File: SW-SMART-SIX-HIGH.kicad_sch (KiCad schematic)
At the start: 53 parts, among them J1 SWLINK, J2 USART1, J3 POWER OUT, J4 POWER IN, SW0 BTS7002-1EPP, SW1 BTS7002-1EPP, SW2 BTS7002-1EPP, U1 STM32G0B1KBTx, U4 MCP2562-E-SN

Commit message: lots of work to do!
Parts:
- removed CVIN1: 10u, Capacitor_SMD:C_1206_3216Metric_Pad1.33x1.80mm_HandSolder, symbol Device:C_Small
- removed VR5V0: NCV1117ST50, PCM_SparkFun-Semiconductor-Standard:SOT-223-3_TabPin2, symbol PCM_SparkFun-Regulator:LM1117-3.3
- added C15, CIN2: 100n, Capacitor_SMD:C_0603_1608Metric_Pad1.08x0.95mm_HandSolder, symbol Device:C_Small
- added CIN1: 10u, Capacitor_SMD:C_1210_3225Metric_Pad1.33x2.70mm_HandSolder, symbol Device:C_Small
- added COUT3, COUT4: 10u, Capacitor_SMD:C_0805_2012Metric_Pad1.18x1.45mm_HandSolder, symbol Device:C_Small
- added COUT5, COUT6, COUT7: 10n, Capacitor_SMD:C_0603_1608Metric_Pad1.08x0.95mm_HandSolder, symbol Device:C_Small
- added J5: POWER OUT, TerminalBlock_Phoenix:TerminalBlock_Phoenix_MKDS-3-5-5.08_1x05_P5.08mm_Horizontal, symbol Connector:Screw_Terminal_01x05
- added L1: 8.2 uH 55.2 mOhm, SRP5030HMT2R2M, symbol SamacSys_Parts:SRP5030HMT-8R2M
- added R13, R14, R16, R17, R19, R20: 4K7, Resistor_SMD:R_0603_1608Metric_Pad0.98x0.95mm_HandSolder, symbol Device:R_Small_US
- added R15, R18, R21: 10K, Resistor_SMD:R_0603_1608Metric_Pad0.98x0.95mm_HandSolder, symbol Device:R_Small_US
- added R22, R23, R24: 1K0, Resistor_SMD:R_0603_1608Metric_Pad0.98x0.95mm_HandSolder, symbol Device:R_Small_US
- added RFBT1: 115K, Resistor_SMD:R_0603_1608Metric_Pad0.98x0.95mm_HandSolder, symbol Device:R_US
- added RGND3, RGND4, RGND5: 47R, Resistor_SMD:R_0603_1608Metric_Pad0.98x0.95mm_HandSolder, symbol Device:R_Small_US
- added RPD3, RPD4, RPD5: 47K, Resistor_SMD:R_0603_1608Metric_Pad0.98x0.95mm_HandSolder, symbol Device:R_Small_US
- added RRFBB1: 22K1, Resistor_SMD:R_0603_1608Metric_Pad0.98x0.95mm_HandSolder, symbol Device:R_US
- added SW3, SW4, SW5: BTS7002-1EPP, SamacSys_Parts:SOP65P600X115-15N, symbol Power_Management:BTS7004-1EPP
- added U3: LMR54410, Package_TO_SOT_SMD:SOT-23-6, symbol Regulator_Switching:LMR50410
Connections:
- net +12V: now also CIN1.1, CIN2.1, SW3.15 (VS), SW4.15 (VS), SW5.15 (VS), U3.4 (EN), U3.5 (VIN)
- net +5V: now also COUT3.1, COUT4.1, L1.2, RFBT1.1
- net GND: now also CIN1.2, CIN2.2, COUT3.2, COUT4.2, COUT5.2, COUT6.2, COUT7.2, R22.1, R23.1, R24.1, RGND3.2, RGND4.2, RGND5.2, RPD3.1, RPD4.1, RPD5.1, RRFBB1.1, U3.2 (GND)
- net SW0DEN: now also R20.1; no longer R10.1, U1.31 (PB7)
- net SW0IN: now also R19.1; no longer R8.1, U1.32 (PB8)
- net SW0IS: now also R21.1; no longer R11.1, U1.9 (PA2)
- net SW2DEN: now also R17.1; no longer R2.1, U1.27 (PB3)
- net SW2IN: now also R16.1; no longer R1.1, U1.28 (PB4)
- net SW2IS: now also R18.1; no longer R6.1, U1.8 (PA1)
- net SW0IS_PD renamed SWIS_PD0
- net SW0OUT renamed SWOUT0
- net SWOUT0: no longer J3.5 (Pin_5)
- net SW1DEN renamed SWDEN1
- net SW1IN renamed SWIN1
- net SW1IS renamed SWIS1
- net SW1IS_PD renamed SWIS_PD1
- net SW1OUT renamed SWOUT1
- net SWOUT1: no longer J3.3 (Pin_3)
- net SW2IS_PD renamed SWIS_PD2
- net SW2OUT renamed SWOUT2
- net SWOUT2: no longer J3.1 (Pin_1)
- new net: RGND5.1, SW5.1 (GND)
- new net: RGND3.1, SW3.1 (GND)
- new net: R13.2, SW3.2 (IN)
- new net: R14.2, SW3.3 (DEN)
- new net: R19.2, SW5.2 (IN)
- new net: R20.2, SW5.3 (DEN)
- new net: RGND4.1, SW4.1 (GND)
- new net: R16.2, SW4.2 (IN)
- new net: R17.2, SW4.3 (DEN)
- new net: RFBT1.2, RRFBB1.2, U3.3 (FB)
- new net CB: C15.1, U3.1 (CB)
- new net SW: C15.2, L1.1, U3.6 (SW)
- new net SW3DEN: R14.1
- new net SW3IN: R13.1
- new net SW3IS: R15.1
- new net SWDEN0: R10.1, U1.31 (PB7)
- new net SWDEN2: R2.1, U1.27 (PB3)
- new net SWIN0: R8.1, U1.32 (PB8)
- new net SWIN2: R1.1, U1.28 (PB4)
- new net SWIS0: R11.1, U1.9 (PA2)
- new net SWIS2: R6.1, U1.8 (PA1)
- new net SWIS_PD3: R15.2, R22.2, SW3.4 (IS)
- new net SWIS_PD4: R18.2, R23.2, SW4.4 (IS)
- new net SWIS_PD5: R21.2, R24.2, SW5.4 (IS)
- new net SWOUT3: COUT5.1, RPD3.2, SW3.10 (OUT), SW3.12 (OUT), SW3.13 (OUT), SW3.14 (OUT), SW3.8 (OUT), SW3.9 (OUT)
- new net SWOUT4: COUT6.1, RPD4.2, SW4.10 (OUT), SW4.12 (OUT), SW4.13 (OUT), SW4.14 (OUT), SW4.8 (OUT), SW4.9 (OUT)
- new net SWOUT5: COUT7.1, RPD5.2, SW5.10 (OUT), SW5.12 (OUT), SW5.13 (OUT), SW5.14 (OUT), SW5.8 (OUT), SW5.9 (OUT)
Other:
- title: Smart Triple High Side Switch -> Smart Six Way High Side Switch
- moved on the sheet: COUT0, H1, H2, H3, H4, R10, R11, R12, R8, RGND0, RPD0, SW0

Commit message: added ACS712 to monitor total board current
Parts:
- added H5, H6: M4 4.3mm, MountingHole:MountingHole_4.3mm_M4, symbol Mechanical:MountingHole
- added U2: ACS71240LLCBTR-050B3, Package_SO:SOIC-8_3.9x4.9mm_P1.27mm, symbol Sensor_Current:ACS712xLCTR-30A
- J1: footprint PCM_SparkFun-Connector:1x05_P2.54mm_Locking -> Connector_PinHeader_2.54mm:PinHeader_1x05_P2.54mm_Vertical
- J2: footprint PCM_SparkFun-Connector:1x04_P2.54mm_Locking -> Connector_PinHeader_2.54mm:PinHeader_1x04_P2.54mm_Vertical
- renumbered COUT3 to C5V2, COUT4 to C5V3, COUT5 to COUT3, COUT6 to COUT4, COUT7 to COUT5
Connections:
- net +12V: now also U2.3 (IP-), U2.4 (IP-); no longer D1.2 (A2), J4.1, J4.2
- net +3.3V: now also U2.8 (VCC)
- net GND: now also U2.5 (GND)
- net SWOUT0: now also J3.5 (Pin_5)
- net SWOUT1: now also J3.3 (Pin_3)
- net SWOUT2: now also J3.1 (Pin_1)
- net SWOUT3: now also J5.1 (Pin_1)
- net SWOUT4: now also J5.3 (Pin_3)
- net SWOUT5: now also J5.5 (Pin_5)
- net IS_TOT: now reaches U1.11 (PA4)
- net IS_TOT: now also U2.7 (VIOUT)
- net SW0DEN renamed SWDEN5
- net SW0IN renamed SWIN5
- net SW0IS renamed SWIS5
- net SW2DEN renamed SWDEN4
- net SW2IN renamed SWIN4
- net SW2IS renamed SWIS4
- net SW3DEN renamed SWDEN3
- net SW3IN renamed SWIN3
- net SW3IS renamed SWIS3
- new net VBAT: D1.2 (A2), J4.1, J4.2, U2.1 (IP+), U2.2 (IP+)
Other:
- moved on the sheet: D1

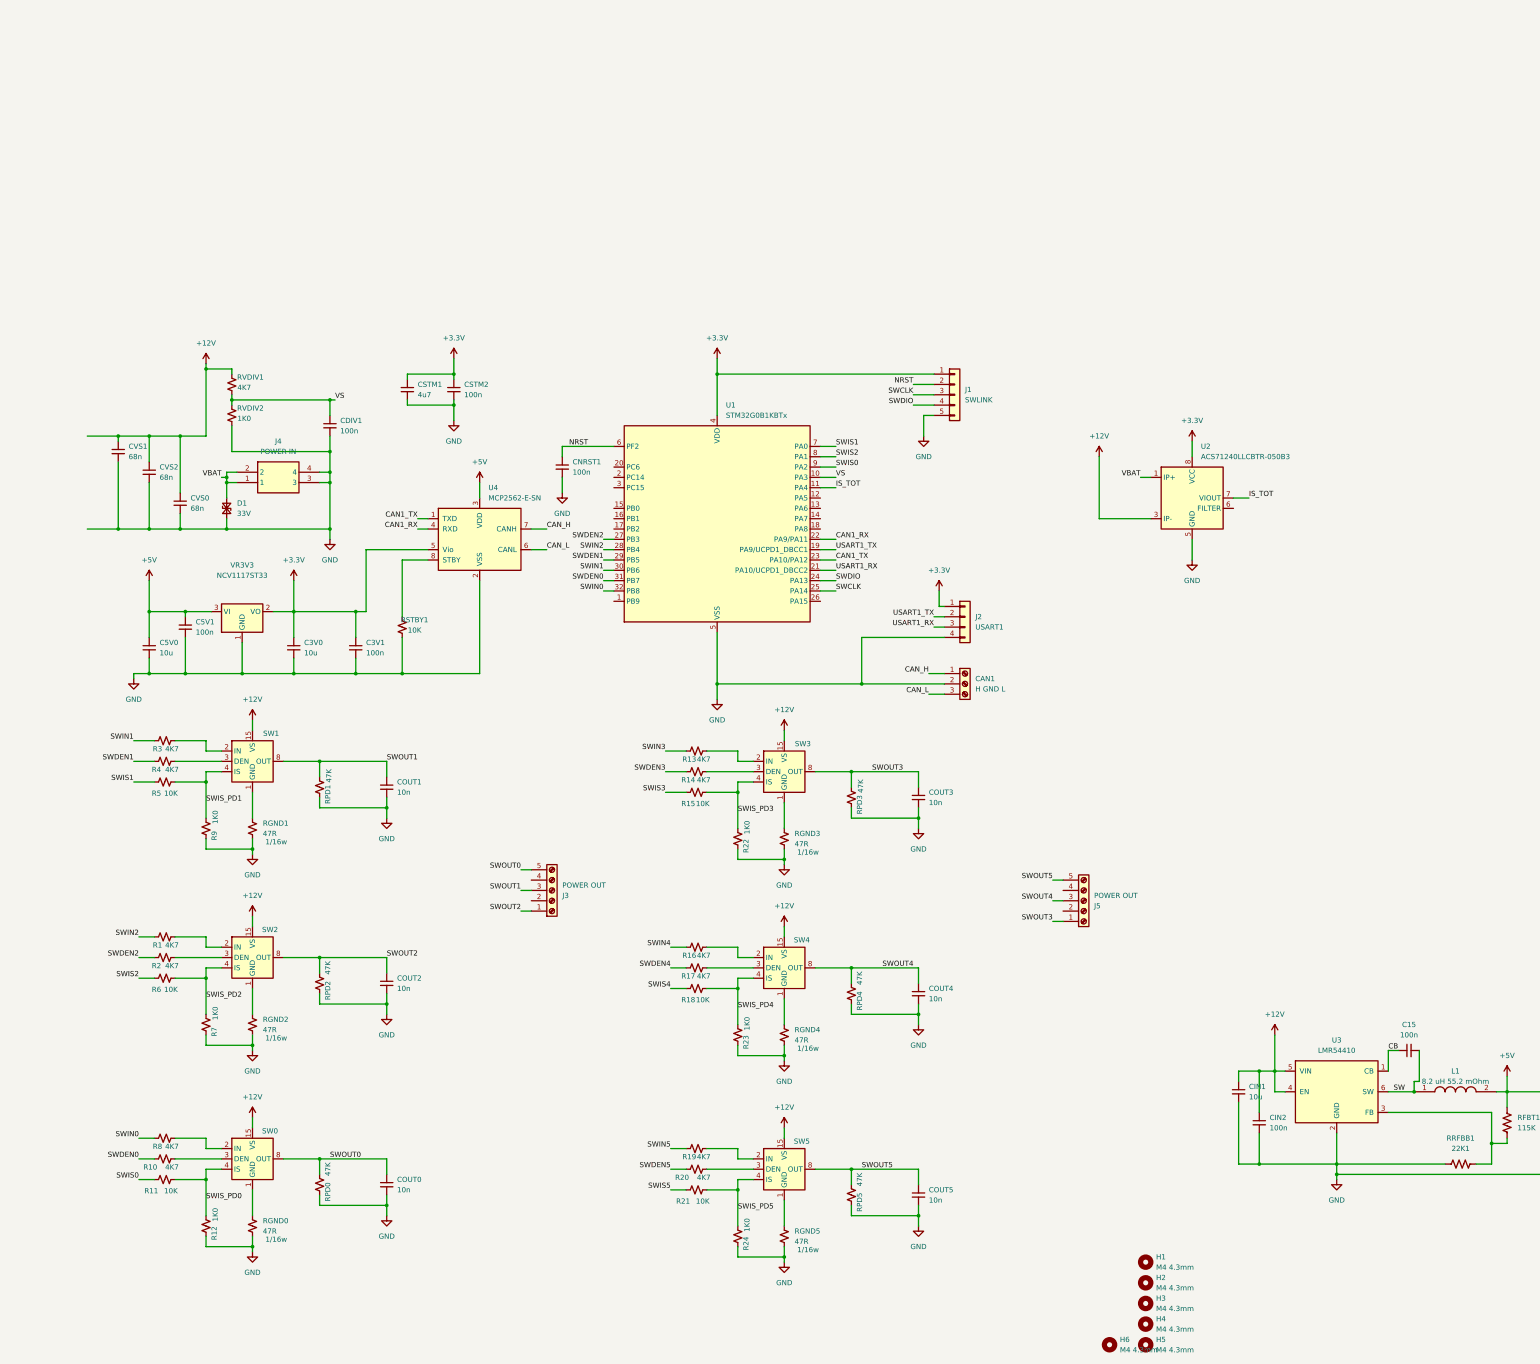
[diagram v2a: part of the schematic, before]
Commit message: swapped to a 48pin uC
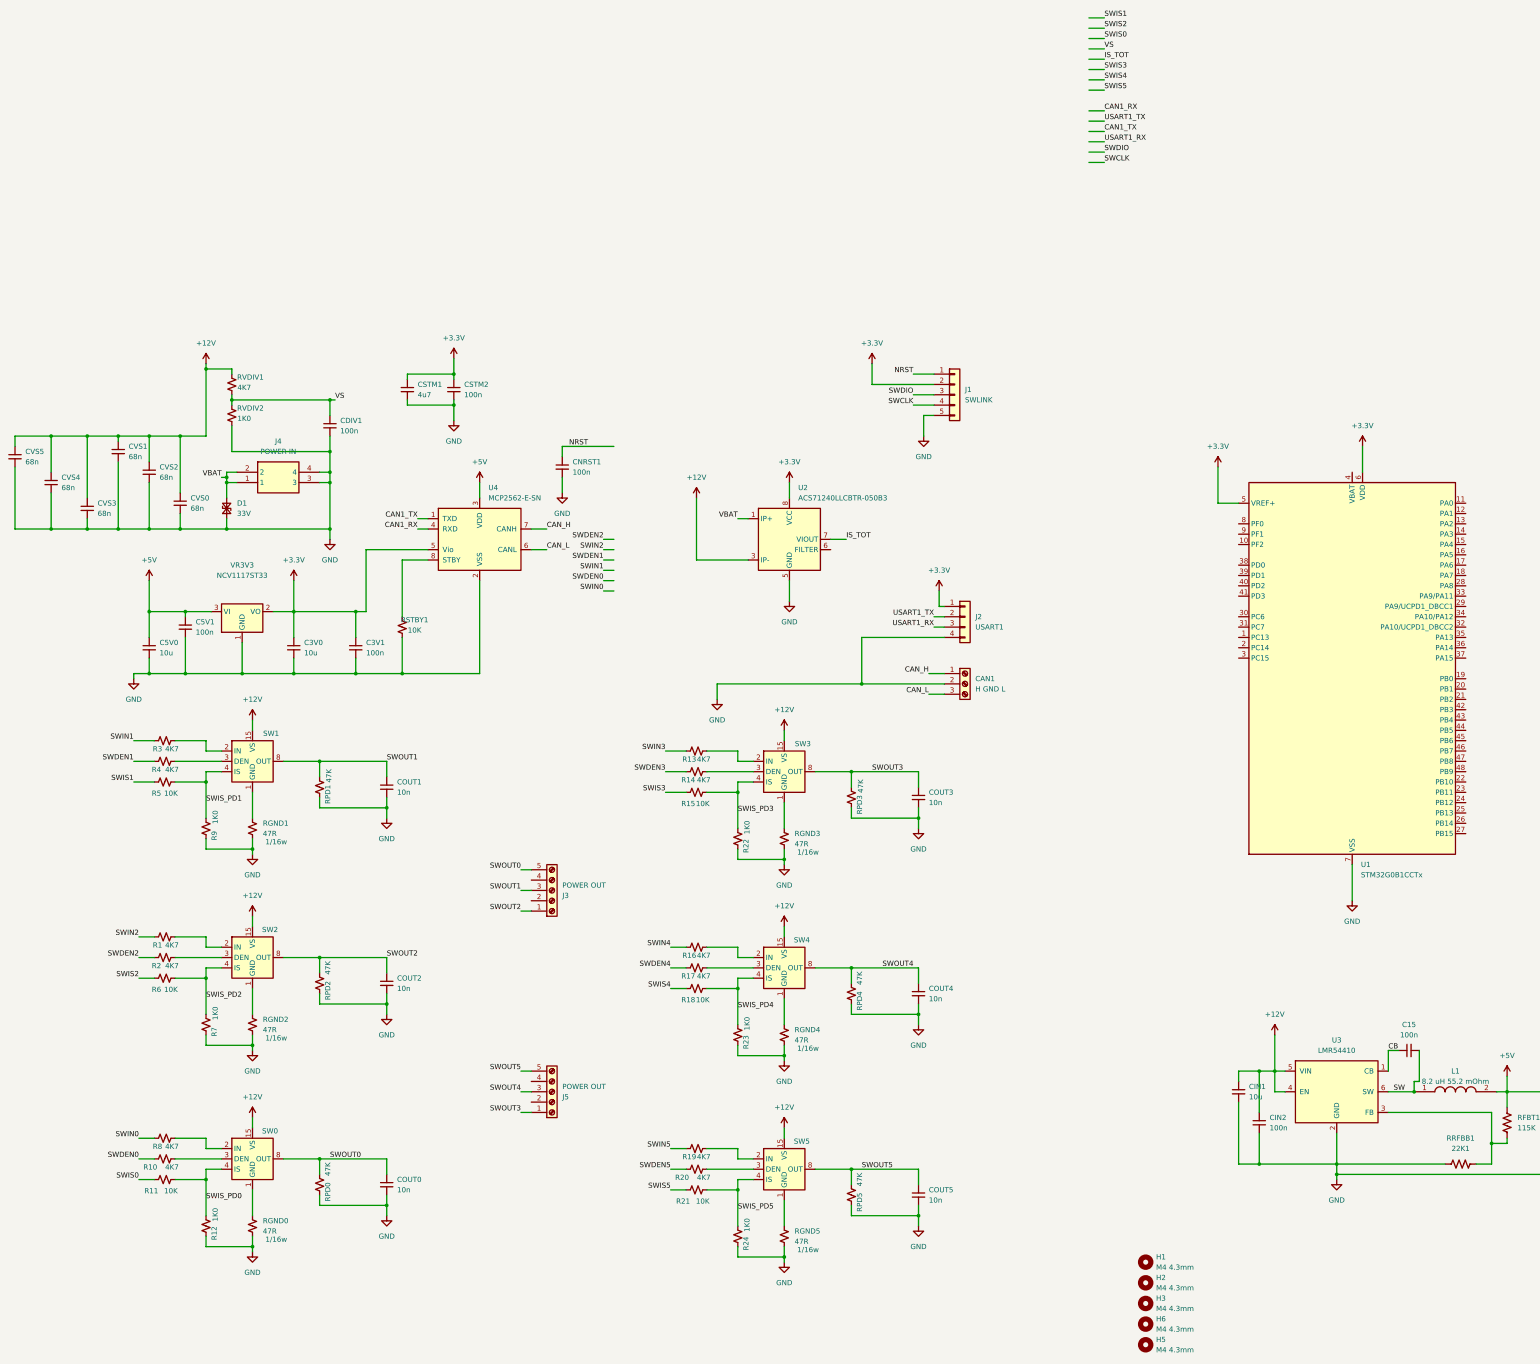
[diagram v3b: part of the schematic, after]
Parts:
- removed H4: M4 4.3mm, MountingHole:MountingHole_4.3mm_M4, symbol Mechanical:MountingHole
- removed U1: STM32G0B1KBTx, Package_QFP:LQFP-32_7x7mm_P0.8mm, symbol MCU_ST_STM32G0:STM32G0B1KBTx
- added CVS3, CVS4, CVS5: 68n, Capacitor_SMD:C_0603_1608Metric_Pad1.08x0.95mm_HandSolder, symbol Device:C_Small
- added U1: STM32G0B1CCTx, Package_QFP:LQFP-48_7x7mm_P0.5mm, symbol MCU_ST_STM32G0:STM32G0B1CCTx
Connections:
- net +12V: now also CVS3.1, CVS4.1, CVS5.1
- net +3.3V: now also J1.2 (Pin_2), U1.5 (VREF+), U1.6 (VDD); no longer J1.1 (Pin_1)
- net GND: now also CVS3.2, CVS4.2, CVS5.2, U1.7 (VSS)
- net NRST: now also J1.1 (Pin_1); no longer J1.2 (Pin_2)
- net SWCLK: now also J1.4 (Pin_4); no longer J1.3 (Pin_3)
- net SWDIO: now also J1.3 (Pin_3); no longer J1.4 (Pin_4)
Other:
- moved on the sheet: H6, J5, U2

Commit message: lots of work to do still
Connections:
- net CAN1_RX: no longer U4.4 (RXD)
- net CAN1_TX: no longer U4.1 (TXD)
- net NRST: now also U1.10 (PF2)
- net SWDEN0: now also U1.13 (PA2)
- net SWIN0: now also U1.14 (PA3)
- net SWIS0: now also U1.12 (PA1)
- net SWIS1: now also U1.11 (PA0)
- net USART1_RX: now also U1.26 (PB14)
- net USART1_TX: now also U1.25 (PB13)
- net CAN_RX: now reaches U1.19 (PB0)
- net CAN_RX: now also U4.4 (RXD)
- net CAN_TX: now reaches U1.20 (PB1)
- net CAN_TX: now also U4.1 (TXD)
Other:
- note added: "22 PB10 A11 23 PB11 A15 24 PB12 A16 25 PC4 A17 UART1_TX 26 PC5 A18 UART1_RX 15 PB0 A8 16 PB1 A9 17 PB2 A10 07 PA0 A0 08 PA1 A1 09 PA2 A2 10 PA3 A3 11 PA4 A4 12 PA5 A5 13 PA6 A6 14 PA7 A7"
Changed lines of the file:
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@@
 		(company "Gordon McLellan")
 	)
+	(text "22 PB10 A11\n23 PB11 A15\n24 PB12 A16\n\n25 PC4 A17 UART1_TX\n26 PC5 A18 UART1_RX\n\n15 PB0 A8\n16 PB1 A9\n17 PB2 A10\n\n07 PA0 A0\n08 PA1 A1\n09 PA2 A2\n10 PA3 A3\n11 PA4 A4\n12 PA5 A5\n13 PA6 A6\n14 PA7 A7"
+		(exclude_from_sim no)
+		(at 298.704 155.702 0)
+		(effects
+			(font
+				(size 1.27 1.27)
+			)
+		)
+	)
 	(junction
 		(at 92.71 41.91)
@@
 	(wire
 		(pts
+			(xy 311.15 64.77) (xy 316.23 64.77)
+		)
+		(stroke
+			(width 0)
+			(type default)
+		)
+	)
+	(wire
+		(pts
 			(xy 33.02 38.1) (xy 33.02 53.34)
 		)
@@
 	(wire
 		(pts
+			(xy 372.11 57.15) (xy 375.92 57.15)
+		)
+		(stroke
+			(width 0)
+			(type default)
+		)
+	)
+	(wire
+		(pts
 			(xy 114.3 58.42) (xy 116.84 58.42)
 		)
@@
 	(wire
 		(pts
+			(xy 372.11 97.79) (xy 375.92 97.79)
+		)
+		(stroke
+			(width 0)
+			(type default)
+		)
+	)
+	(wire
+		(pts
 			(xy 57.15 87.63) (xy 57.15 96.52)
 		)
@@
 	(wire
 		(pts
+			(xy 372.11 133.35) (xy 375.92 133.35)
+		)
+		(stroke
+			(width 0)
+			(type default)
+		)
+	)
+	(wire
+		(pts
 			(xy 139.7 199.39) (xy 142.24 199.39)
 		)
@@
 	(wire
 		(pts
+			(xy 372.11 100.33) (xy 375.92 100.33)
+		)
+		(stroke
+			(width 0)
+			(type default)
+		)
+	)
+	(wire
+		(pts
 			(xy 78.74 81.28) (xy 83.82 81.28)
 		)
@@
 	(wire
 		(pts
+			(xy 372.11 62.23) (xy 375.92 62.23)
+		)
+		(stroke
+			(width 0)
+			(type default)
+		)
+	)
+	(wire
+		(pts
 			(xy 401.32 213.36) (xy 401.32 210.82)
 		)
@@
 	(wire
 		(pts
+			(xy 372.11 59.69) (xy 375.92 59.69)
+		)
+		(stroke
+			(width 0)
+			(type default)
+		)
+	)
+	(wire
+		(pts
 			(xy 81.28 166.37) (xy 90.17 166.37)
 		)
@@
 	(wire
 		(pts
+			(xy 372.11 54.61) (xy 375.92 54.61)
+		)
+		(stroke
+			(width 0)
+			(type default)
+		)
+	)
+	(wire
+		(pts
 			(xy 62.23 20.32) (xy 62.23 21.59)
 		)
@@
 	(wire
 		(pts
+			(xy 372.11 130.81) (xy 375.92 130.81)
+		)
+		(stroke
+			(width 0)
+			(type default)
+		)
+	)
+	(wire
+		(pts
 			(xy 401.32 219.71) (xy 401.32 213.36)
 		)
@@
 		)
 	)
+	(label "CAN_TX"
+		(at 375.92 100.33 0)
+		(effects
+			(font
+				(size 1.27 1.27)
+			)
+			(justify left bottom)
+		)
+	)
 	(label "SWIS0"
 		(at 45.72 220.98 180)
@@
 		)
 	)
-	(label "CAN1_RX"
+	(label "CAN_RX"
 		(at 114.3 60.96 180)
 		(effects
@@
 		)
 	)
+	(label "SWIN0"
+		(at 375.92 62.23 0)
+		(effects
+			(font
+				(size 1.27 1.27)
+			)
+			(justify left bottom)
+		)
+	)
+	(label "SWDEN0"
+		(at 375.92 59.69 0)
+		(effects
+			(font
+				(size 1.27 1.27)
+			)
+			(justify left bottom)
+		)
+	)
 	(label "VBAT"
 		(at 193.04 58.42 180)
@@
 		)
 	)
+	(label "USART1_TX"
+		(at 375.92 130.81 0)
+		(effects
+			(font
+				(size 1.27 1.27)
+			)
+			(justify left bottom)
+		)
+	)
 	(label "NRST"
 		(at 156.21 40.64 180)
@@
 		)
 	)
+	(label "SWIS1"
+		(at 375.92 54.61 0)
+		(effects
+			(font
+				(size 1.27 1.27)
+			)
+			(justify left bottom)
+		)
+	)
 	(label "SWIS4"
 		(at 176.53 173.99 180)
@@
 		)
 	)
+	(label "USART1_RX"
+		(at 375.92 133.35 0)
+		(effects
+			(font
+				(size 1.27 1.27)
+			)
+			(justify left bottom)
+		)
+	)
+	(label "SWIS0"
+		(at 375.92 57.15 0)
+		(effects
+			(font
+				(size 1.27 1.27)
+			)
+			(justify left bottom)
+		)
+	)
 	(label "SWOUT5"
 		(at 139.7 194.31 180)
@@
 		)
 	)
+	(label "NRST"
+		(at 311.15 64.77 180)
+		(effects
+			(font
+				(size 1.27 1.27)
+			)
+			(justify right bottom)
+		)
+	)
 	(label "USART1_RX"
 		(at 283.21 -34.29 0)
@@
 		)
 	)
-	(label "CAN1_TX"
+	(label "CAN_TX"
 		(at 114.3 58.42 180)
 		(effects
@@
 		)
 	)
+	(label "CAN_RX"
+		(at 375.92 97.79 0)
+		(effects
+			(font
+				(size 1.27 1.27)
+			)
+			(justify left bottom)
+		)
+	)
